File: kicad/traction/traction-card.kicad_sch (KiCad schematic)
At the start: 301 parts, among them Y1 CX3225GA40000D0PTVCC

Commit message: Rev A.17: round 18 — three rechecks of 4425af9 (F190-F198): diversion diodes on the amplifier node (loop passes RSX), diode cell cathode = pin 1 on all 35 diodes, exciter TVS/PTC rows at worst corners + ECU-asleep sustained short (WARN rows, layout rule, QP-RX-04 2b gate), anti-surge RSX, NCV4276C reverse current = QP-RX-05 gate + VR-33, IR-16/IR-42, firmware FW-34..36 (sample freshness, cadence-locked resolver frames, latency sign) + three self-found instances
Co-Authored-By: Claude Fable 5.1 <noreply@anthropic.com>
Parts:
- DBAT, DCLR, DEXN, DEXP, DFLT1, DFLT2, DFO, DIGN, DREVC, DTVSC, DTVSC2, ZLVS, ZSET: symbol traction:D -> traction:D_21
- RSXN, RSXP: MPN ERJ-8ENF2R20V -> ESR18EZPF2R20
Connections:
- net ASC_SET_N: now also ZSET.1; no longer ZSET.2
- net BATSNS: now also DBAT.1; no longer DBAT.2
- net DGND: now also DTVSC2.1, ZSET.2; no longer DTVSC2.2, ZSET.1
- net FAULT_OUT: now also DFO.2; no longer DFO.1
- net FCO: now also DREVC.2, DTVSC.1; no longer DREVC.1, DTVSC.2
- net FLT_CLR_N: now also DCLR.2; no longer DCLR.1
- net FLT_CMB_N: now also DFLT1.2, DFLT2.2; no longer DFLT1.1, DFLT2.1
- net FLT_HS_N: now also DFLT1.1; no longer DFLT1.2
- net FLT_LS_N: now also DFLT2.1; no longer DFLT2.2
- net FOUT_K: now also DFO.1; no longer DFO.2
- net IGN_D: now also DIGN.1; no longer DIGN.2
- net KL15: now also DIGN.2; no longer DIGN.1
- net LVS_G: now also ZLVS.2; no longer ZLVS.1
- net NRC: now also DREVC.1, ZLVS.1; no longer DREVC.2, ZLVS.2
- net TVSM: now also DTVSC.2, DTVSC2.2; no longer DTVSC.1, DTVSC2.1
- net V5A: now also DCLR.1; no longer DCLR.2
- net VBATC: now also DBAT.2; no longer DBAT.1
- net VEXD: now also DEXN.1, DEXP.1; no longer DEXN.2, DEXP.2
- net VREX_N: now also DEXN.2
- net VREX_NX: no longer DEXN.1
- net VREX_P: now also DEXP.2
- net VREX_PX: no longer DEXP.1
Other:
- note added: "rev A.17 - 26 sections - 301 components"
- note removed: "rev A.16 - 26 sections - 301 components"
- moved on the sheet: CEXA1, CEXA2, CEXA3, CEXA4, FEXN, FEXP, REXA1, REXA2, REXA3, REXA4, RSXN, RSXP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

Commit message: Rev A.18: round 19 — three rechecks of e315bf1 (F199-F204): PTC-current row at every permitted voltage (IR-16 0.08/0.14/0.37/0.26 Ω), ≥8 A TVS energy an explicit assumption + QP-RX-04 release criterion, window criterion fixed, exciter TVS → SMDJ7.0A-HRA (coupled island holds the 7.0 V class at a parked 12 V battery / the Marine rail), shared exciter-fault model run for the Marine port (QP-MA-11, kit-loom rule), FW-35 rewritten on an SWG-anchored time origin with clock-derived resync and bounded restart
Co-Authored-By: Claude Fable 5.1 <noreply@anthropic.com>
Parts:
- TVSEN, TVSEP: value SMDJ8.5A-HRA -> SMDJ7.0A-HRA; MPN SMDJ8.5A-HRA -> SMDJ7.0A-HRA
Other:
- note added: "rev A.18 - 26 sections - 301 components"
- note removed: "rev A.17 - 26 sections - 301 components"
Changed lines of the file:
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@@
 		(title "Traction Inverter — Control Card (S32K396 + FS26, ASIL D)")
 		(date "2026-09-23")
-		(rev "A.17")
+		(rev "A.18")
 		(company "Traction Inverter 220 kW pk - Control card (LV), sheet 4 of 4")
 		(comment 1 "Inverter = Power board + Cap bank busbar + bolt-on Discharge board (all HV) + Control card (LV); safe state holds with any link lost")
@@
 		(exclude_from_sim no) (in_bom yes) (on_board yes) (dnp no)
 		(property "Reference" "TVSEN" (at 849.63 173.736 0) (effects (font (size 1.27 1.27))))
-		(property "Value" "SMDJ8.5A-HRA" (at 849.63 182.118 0) (effects (font (size 1.27 1.27))))
+		(property "Value" "SMDJ7.0A-HRA" (at 849.63 182.118 0) (effects (font (size 1.27 1.27))))
 		(property "Footprint" "SMC" (at 849.63 177.8 0) (effects (font (size 1.27 1.27)) (hide yes)))
 		(property "Datasheet" "~" (at 849.63 177.8 0) (effects (font (size 1.27 1.27)) (hide yes)))
 		(property "LCSC" "CLASS" (at 849.63 177.8 0) (effects (font (size 1.27 1.27)) (hide yes)))
-		(property "MPN" "SMDJ8.5A-HRA" (at 849.63 177.8 0) (effects (font (size 1.27 1.27)) (hide yes)))
+		(property "MPN" "SMDJ7.0A-HRA" (at 849.63 177.8 0) (effects (font (size 1.27 1.27)) (hide yes)))
 		(instances (project "traction" (path "/05063e63-3076-48d3-a84c-7e92d29634e7/073bda8d-ada5-42f5-b7f9-206abe13de00" (reference "TVSEN") (unit 1)) (path "/806594cd-32aa-475d-95e3-87c882c626ff" (reference "TVSEN") (unit 1))))
 	)
@@
 		(exclude_from_sim no) (in_bom yes) (on_board yes) (dnp no)
 		(property "Reference" "TVSEP" (at 849.63 143.256 0) (effects (font (size 1.27 1.27))))
-		(property "Value" "SMDJ8.5A-HRA" (at 849.63 151.638 0) (effects (font (size 1.27 1.27))))
+		(property "Value" "SMDJ7.0A-HRA" (at 849.63 151.638 0) (effects (font (size 1.27 1.27))))
 		(property "Footprint" "SMC" (at 849.63 147.32 0) (effects (font (size 1.27 1.27)) (hide yes)))
 		(property "Datasheet" "~" (at 849.63 147.32 0) (effects (font (size 1.27 1.27)) (hide yes)))
 		(property "LCSC" "CLASS" (at 849.63 147.32 0) (effects (font (size 1.27 1.27)) (hide yes)))
-		(property "MPN" "SMDJ8.5A-HRA" (at 849.63 147.32 0) (effects (font (size 1.27 1.27)) (hide yes)))
+		(property "MPN" "SMDJ7.0A-HRA" (at 849.63 147.32 0) (effects (font (size 1.27 1.27)) (hide yes)))
 		(instances (project "traction" (path "/05063e63-3076-48d3-a84c-7e92d29634e7/073bda8d-ada5-42f5-b7f9-206abe13de00" (reference "TVSEP") (unit 1)) (path "/806594cd-32aa-475d-95e3-87c882c626ff" (reference "TVSEP") (unit 1))))
 	)
@@
 	(text "CARD-IF   -   1 section" (exclude_from_sim no) (at 849.63 548.64 0) (effects (font (size 1.524 1.524)) (justify left bottom)))
 	(text "VEHICLE-IF   -   1 section" (exclude_from_sim no) (at 849.63 556.26 0) (effects (font (size 1.524 1.524)) (justify left bottom)))
-	(text "rev A.17   -   26 sections   -   301 components" (exclude_from_sim no) (at 849.884 572.77 0) (effects (font (size 1.524 1.524)) (justify left bottom)))
+	(text "rev A.18   -   26 sections   -   301 components" (exclude_from_sim no) (at 849.884 572.77 0) (effects (font (size 1.524 1.524)) (justify left bottom)))
 	(text "NET NAMING" (exclude_from_sim no) (at 849.884 600.964 0) (effects (font (size 2.0066 2.0066) (bold yes)) (justify left bottom)))
 	(text "internal junctions are named for what they join" (exclude_from_sim no) (at 849.884 607.568 0) (effects (font (size 1.524 1.524)) (justify left bottom)))

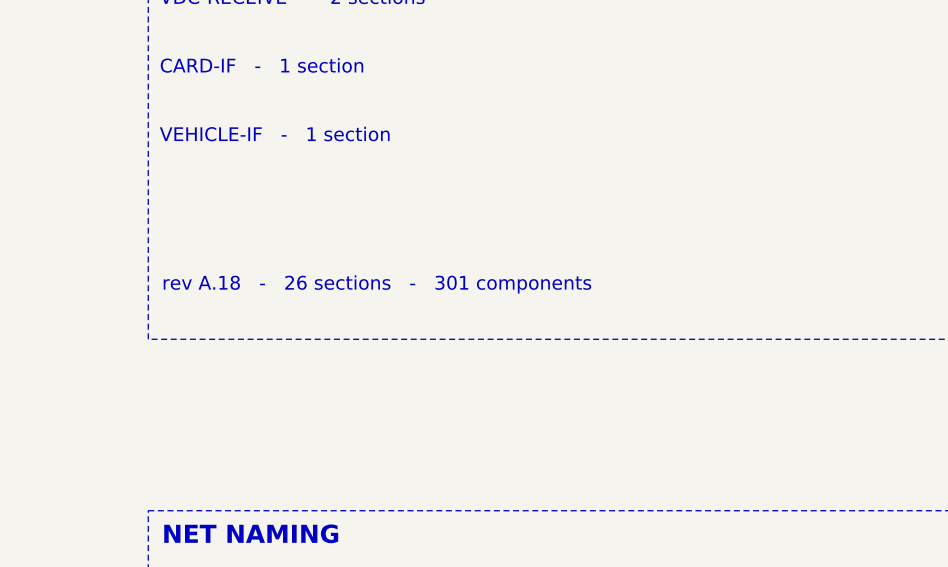
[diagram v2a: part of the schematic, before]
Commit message: Rev A.19: round 20 — three rechecks of 00f6252 (F205-F207): TVS alternate to the 7.0 V class + lock, 4XX discharge alternate 470→220 Ω + lock, T-05/T-06 firmware ID, 8.5 V-era figures re-derived at the IR-16 allocations
Co-Authored-By: Claude Fable 5.1 <noreply@anthropic.com>
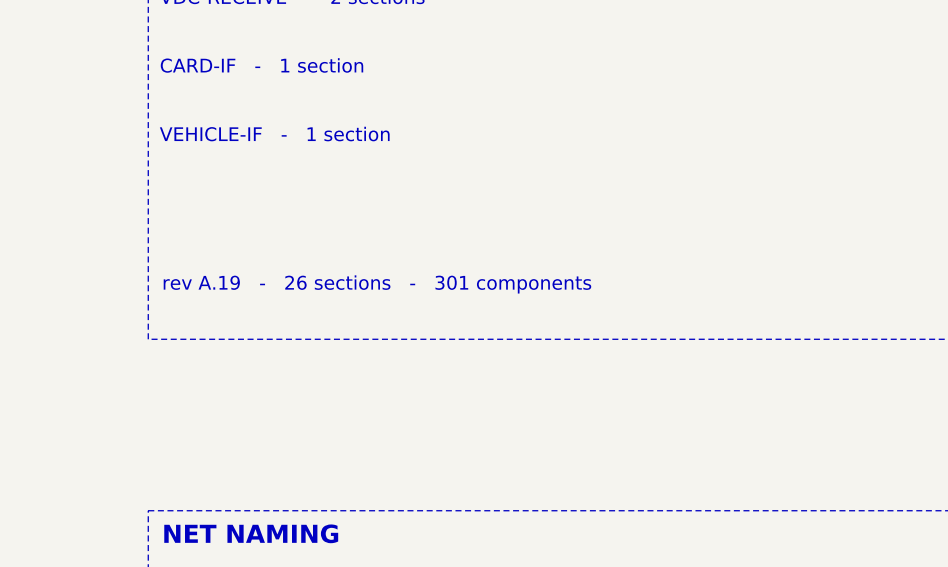
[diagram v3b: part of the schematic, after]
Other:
- note added: "rev A.19 - 26 sections - 301 components"
- note removed: "rev A.18 - 26 sections - 301 components"
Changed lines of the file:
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@@
 		(title "Traction Inverter — Control Card (S32K396 + FS26, ASIL D)")
 		(date "2026-09-23")
-		(rev "A.18")
+		(rev "A.19")
 		(company "Traction Inverter 220 kW pk - Control card (LV), sheet 4 of 4")
 		(comment 1 "Inverter = Power board + Cap bank busbar + bolt-on Discharge board (all HV) + Control card (LV); safe state holds with any link lost")
@@
 	(text "CARD-IF   -   1 section" (exclude_from_sim no) (at 849.63 548.64 0) (effects (font (size 1.524 1.524)) (justify left bottom)))
 	(text "VEHICLE-IF   -   1 section" (exclude_from_sim no) (at 849.63 556.26 0) (effects (font (size 1.524 1.524)) (justify left bottom)))
-	(text "rev A.18   -   26 sections   -   301 components" (exclude_from_sim no) (at 849.884 572.77 0) (effects (font (size 1.524 1.524)) (justify left bottom)))
+	(text "rev A.19   -   26 sections   -   301 components" (exclude_from_sim no) (at 849.884 572.77 0) (effects (font (size 1.524 1.524)) (justify left bottom)))
 	(text "NET NAMING" (exclude_from_sim no) (at 849.884 600.964 0) (effects (font (size 2.0066 2.0066) (bold yes)) (justify left bottom)))
 	(text "internal junctions are named for what they join" (exclude_from_sim no) (at 849.884 607.568 0) (effects (font (size 1.524 1.524)) (justify left bottom)))

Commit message: Rev A.20: round 21 — three rechecks of 551c405 (F208): stale 0.29 Ω in gate ㉘ and the QP-RX-04 fixture instruction → 0.37 Ω, last 8.5 V-era figures aligned, Marine sweep cross-references at the current values
Co-Authored-By: Claude Fable 5.1 <noreply@anthropic.com>
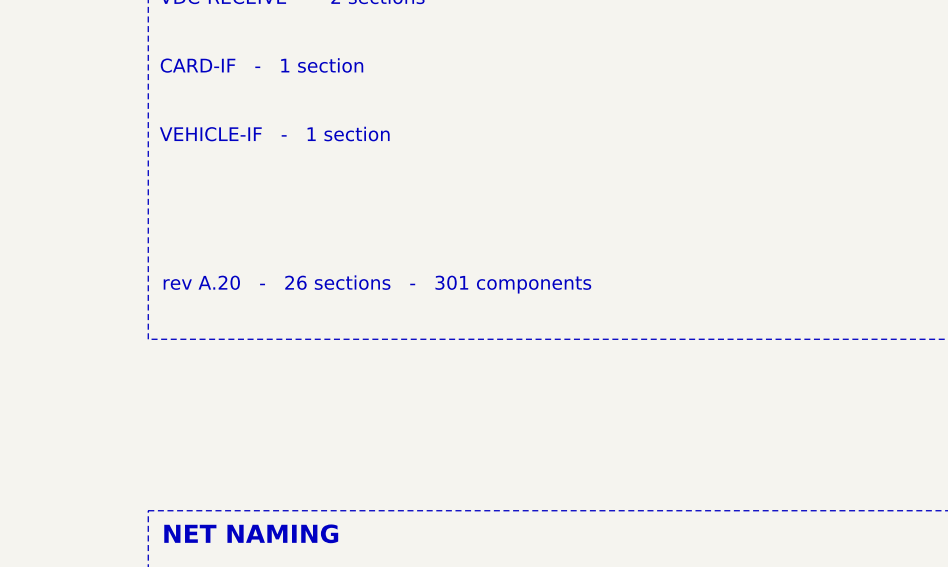
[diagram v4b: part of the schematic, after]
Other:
- note added: "rev A.20 - 26 sections - 301 components"
- note removed: "rev A.19 - 26 sections - 301 components"
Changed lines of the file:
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@@
 		(title "Traction Inverter — Control Card (S32K396 + FS26, ASIL D)")
 		(date "2026-09-23")
-		(rev "A.19")
+		(rev "A.20")
 		(company "Traction Inverter 220 kW pk - Control card (LV), sheet 4 of 4")
 		(comment 1 "Inverter = Power board + Cap bank busbar + bolt-on Discharge board (all HV) + Control card (LV); safe state holds with any link lost")
@@
 	(text "CARD-IF   -   1 section" (exclude_from_sim no) (at 849.63 548.64 0) (effects (font (size 1.524 1.524)) (justify left bottom)))
 	(text "VEHICLE-IF   -   1 section" (exclude_from_sim no) (at 849.63 556.26 0) (effects (font (size 1.524 1.524)) (justify left bottom)))
-	(text "rev A.19   -   26 sections   -   301 components" (exclude_from_sim no) (at 849.884 572.77 0) (effects (font (size 1.524 1.524)) (justify left bottom)))
+	(text "rev A.20   -   26 sections   -   301 components" (exclude_from_sim no) (at 849.884 572.77 0) (effects (font (size 1.524 1.524)) (justify left bottom)))
 	(text "NET NAMING" (exclude_from_sim no) (at 849.884 600.964 0) (effects (font (size 2.0066 2.0066) (bold yes)) (justify left bottom)))
 	(text "internal junctions are named for what they join" (exclude_from_sim no) (at 849.884 607.568 0) (effects (font (size 1.524 1.524)) (justify left bottom)))

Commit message: Rev A.21: round 22 — three rechecks of 0ff44d9 (F209) + the layout handoff (F210–F213): every KiCad symbol bound to a footprint in a shipped traction.pretty (45 verbatim KiCad-10 patterns + 18 datasheet-drawn), fp-lib-table and per-board projects in all sets, pad-per-pin KiCad proof; NCV4276C 5-lead lands, ALM2402/TPS55340 thermal-pad pins, 2-pad crystal; QP §0.2 baseline and stale IDs; docs/layout-handoff.md
Co-Authored-By: Claude Fable 5.1 <noreply@anthropic.com>
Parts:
- CAND1, CAND2, CASCG, CBAL, CBTC, CBTP, CCAN1, CCAN2, CCLR, CCOSA1, CCOSA2, CCOSA3, CCOSD, CCOSF1, CCOSF2, CCT1, CCT2, CEXA1, CEXA2, CEXA3, CEXA4, CEXM, CFLTD, CFLTF, CFLTF2, CIGN, CIGNS, CILK, CLAT, CLAT2, CLDEC, CLVSM, CMA1, CMA2, CMD1, CMD10, CMD11, CMD12, CMD2, CMD3, CMD4, CMD5, CMD6, CMD7, CMD8, CMD9, CMT1F, CMT2F, COF1, COR1, COR2, CRST, CSCH, CSCH2, CSCH3, CSINA1, CSINA2, CSINA3, CSIND, CSINF1, CSINF2, CSNUF, CSNVF, CSNWF, CTAMBF, CTHSF, CUB1, CUB2, CUS1, CUS2, CV25, CVB1, CVB2, CVD1, CVD2, CVDIG, CVM1, CVM2, CVS1, CVS2, CWB1, CWB2, CWS1, CWS2, CYA, CYB: footprint C0603 -> traction:C_0603_1608Metric
- CEXD, CLVC1: footprint C1206 -> traction:C_1206_3216Metric
- CLDE, CLVC2: footprint C1210 -> traction:C_1210_3225Metric
- CLVC3: footprint CAP-ALU-SMD-G-10x10.2 -> traction:CP_Elec_10x10.5
- CSB1, CSB2, CSB3, CSB3B, CSB4, CSB5, CSB6, CSB7, CSB8, CVBOS: footprint C0805 -> traction:C_0805_2012Metric
- DBAT, DCLR, DFLT1, DFLT2, DFO, ZLVS, ZSET: footprint SOD123 -> traction:D_SOD-123
- DCOSP, DSINP, QBAL, QLVN, TVSC1, TVSC2: footprint SOT23 -> traction:SOT-23-3
- DEXN, DEXP: footprint SOD128 -> traction:D_SOD-128
- DIGN, TVSM1, TVSM2: footprint SMA -> traction:D_SMA
- DREVC, DTVSC, DTVSC2, TVSEN, TVSEP: footprint SMC -> traction:D_SMC
- FEXN, FEXP: footprint 1812 -> traction:Fuse_1812_4532Metric
- FLVC: footprint 2410 -> traction:Bel_0680L_2410
- FMT1, FMT2: footprint F0603 -> traction:Fuse_0603_1608Metric
- FVBH, FVBL: footprint PTC2920 -> traction:Fuse_2920_7451Metric
- FVS1: footprint PTC1812 -> traction:Fuse_1812_4532Metric
- JICC: footprint HDR2x20-2.54 -> traction:Samtec_IPL1-120_2x20
- JLEM: footprint HDR2x5 -> traction:PinHeader_2x05_P2.00mm_Vertical
- JSWD: footprint HDR2x5-1.27 -> traction:PinHeader_2x05_P1.27mm_Vertical
- JVEH: footprint AMPSEAL23 -> traction:TE_770669-1
- LCAN1, LCAN2: footprint CMC1210 -> traction:TDK_ACT45B
- LCOR: footprint XAL4020 -> traction:L_Coilcraft_XAL4020-XXX
- LFC: footprint FB1206 -> traction:L_1206_3216Metric
- LSBC: footprint XAL4040 -> traction:L_Coilcraft_XAL4040-XXX
- LUB, LVB, LWB: footprint FB0805 -> traction:L_0805_2012Metric
- LVS1, LVS2, LVS3, LVS4: footprint FB0603 -> traction:L_0603_1608Metric
- QLVS: footprint SOT223 -> traction:SOT-223
- RAGT: footprint R0805 -> traction:R_0805_2012Metric
- RARB, RASCP, RBOOT, RCOS1, RCOS2, RCOSF1, RCOSF2, RCOSR1, RCOSR2, RCPD0, RCPD1, RCPD2, RCPD3, RCT1A, RCT1B, RCT2A, RCT2B, RDBG, RDRB, RENP1, REXA1, REXA2, REXA3, REXA4, REXB1, REXB2, REXB3, REXB4, REXM1, REXM2, REXM3, REXM4, RFCB, RFLTC, RFLTD, RFLTP1, RFLTP2, RFS1, RFS2, RFS3, RGPD, RHWP, RIGN1, RIGN2, RIGNS1, RIGNS2, RILK1, RILK2, RILK3, RILK4, RLAT1, RLAT2, RLDE1, RLDE2, RLVSD, RLVSG, RLVSM, RMRST, RMT1P, RMT1S, RMT2P, RMT2S, ROF1, ROF2, RQDM, RRDB, RRDYP1, RRDYP2, RSB1, RSB2, RSB3, RSB4, RSCH, RSDN, RSIN1, RSIN2, RSINF1, RSINF2, RSINR1, RSINR2, RSNUP, RSNVP, RSNWP, RTAMB, RTAMBP, RTHS, RTHSP, RTMR, RUB0, RUB1, RUB2, RUB3, RV5GP, RV5GS, RVB0, RVB1, RVB2, RVB3, RVD1A, RVD1B, RVD1C, RVD1D, RVD2A, RVD2B, RVD2C, RVD2D, RVM1, RVM2, RVM3, RVM4, RWB0, RWB1, RWB2, RWB3: footprint R0603 -> traction:R_0603_1608Metric
- RFS4, RSXN, RSXP: footprint R1206 -> traction:R_1206_3216Metric
- UAND1, UAND2: footprint SOT363 -> traction:SOT-363_SC-70-6
- UASCG, UOR1, UOR2: footprint SOT353 -> traction:SOT-353_SC-70-5
- UCAN1, UCAN2: footprint SOIC8 -> traction:SOIC-8_3.9x4.9mm_P1.27mm
- UEXD: footprint HTSSOP14-PWP -> traction:ALM2402-Q1_PWP0014H
- UEXF, UMT1, UMT2, UUB1, UUB2, UVB1, UVB2, UVD1, UVD2, UVMB1, UVMB2, UVOF, UWB1, UWB2: footprint SOT23-5 -> traction:SOT-23-5
- ULAT, ULAT2, USCH, USCH2, USCH3: footprint VSSOP8 -> traction:VSSOP-8_2.3x2mm_P0.5mm
- ULDOEX: footprint DPAK5 -> traction:TO-252-5_TabPin3
- UMCU: footprint MAPBGA289 -> traction:MAPBGA-289_14x14mm_Layout17x17_P0.8mm
- USBC: footprint HLQFP48 -> traction:FS26_HLQFP48
- USNSU, USNSV, USNSW: footprint OffBoard -> (none)
- Y1: footprint X3225 -> traction:Kyocera_CX3225GA_2Pad
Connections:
- net AGND: now also UEXD.15 (PAD)
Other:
- note added: "rev A.21 - 26 sections - 301 components"
- note removed: "rev A.20 - 26 sections - 301 components"
- moved on the sheet: CEXD, REXB1, REXB2, REXB3, REXB4, RSDN

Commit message: Rev A.22: round 23 — rechecks of 452de85 (F214–F220), the VESC program (FW-38…FW-46, Traction Tool in Qt) and the "why not done" extension (F221–F239)
Hardware: the R2R reference isolated at ball A9 (RR2R 10 Ω + 1 µF + 100 nF, S32K39 DS note 8), the SWD header on its
surface-mount Samtec land with a mounting-technology lock in the library generator, the footprint library declared
KiCad 10.0.6+ and no longer mirrored into the KiCad 5 sets; the BOM intro follows the SKU; a VREFH window row and VR-34/35.

Firmware (TI_FW_ID 0x0A0F0015, CAL layout 4, 190 fields / 91 CAL rows, 80 DTCs): FW-37 joint torque solve with a
postcondition; the VESC gap closure — FW-38 signed field update (Ed25519, anti-rollback, ISO-TP), FW-39 interlocked motor
self-commissioning, FW-40 UDS diagnostics (0x19/0x22/0x2A/0x14 over ISO 15765-2), FW-41 fault-triggered waveform capture,
FW-42 overspeed, FW-43 run-time statistics, FW-44 key-on offset adoption, FW-45 saturation-dependent inductance tables
with gain scheduling, FW-46 cogging feed-forward; twelve defects found by the closed-loop simulator bridge (F221–F232),
the 64-bit divide out of every ISR path with a link-time guard, the UDS escape single frame accepted by every service,
the root of trust reported (DID 0xFD23), the boot record, motor data and active maps as DIDs; 421 tests / 4937 checks /
0 failed on the host (-O1, -O2, ASan/UBSan, -ffp-contract=off) and on the Cortex-M7 under QEMU with the target compiler
(make qemu-test, T-59); make target-check 63 markers, make target-size with the divide guard.

Traction Tool (tool/): Qt 6 / C++17 Widgets + Qwt, offline; pages Dashboard, Live plots, Controls, Commissioning,
Parameters, Faults & alerts, Analysis, Terminal, Firmware; transports simulator bridge (tool/bridge, the real firmware
against a plant), log replay, CAN (QCanBus with ISO-TP both ways, proved against the firmware over the virtualcan bus);
the signed update end to end over both transports; the commissioning routines, the map sw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
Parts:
- added CR2R1: 1uF, traction:C_0603_1608Metric, symbol traction:C
- added CR2R2: 100nF, traction:C_0603_1608Metric, symbol traction:C
- added RR2R: 10R, traction:R_0603_1608Metric, symbol traction:R
- JSWD: footprint traction:PinHeader_2x05_P1.27mm_Vertical -> traction:Samtec_FTSH-105-01-L-DV-K
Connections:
- net AGND: now also CR2R1.2, CR2R2.2
- net VREF5: now also RR2R.1; no longer UMCU.A9 (A9_VREFH_R2R)
- new net VR2R: CR2R1.1, CR2R2.1, RR2R.2, UMCU.A9 (A9_VREFH_R2R)
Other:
- note added: "rev A.22 - 26 sections - 304 components"
- note removed: "rev A.21 - 26 sections - 301 components"
- moved on the sheet: CAND1, CAND2, CASCG, CBAL, CBTC, CBTP, CCAN1, CCAN2, CCLR, CCOSA1, CCOSA2, CCOSA3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

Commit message: Rev A.23: round 24 — four rechecks of 4ed0101 (F240–F244): the SDADC reference on its supply node, acquisition freshness, the map's flux slope and the ripple limiter's exact bounds, the temperature latch, the V_DC expiry
Hardware (F240, no new part): the S32K39 data sheet's SDADC table (Rev. 3 Table 38, in our archive and our own
extracted-parameters file) requires VREFP within ±25 mV of AVDD; the round-23 disposition had judged the general +100 mV
note and called the figure absent while the references sat on the FS26 VREF, matched to the SDADC-supply LDO only within
±1 %. Every non-R2R reference group (E6/H6 SAR, E10/F13 SDADC) is now on V5A itself with VDDA_SDADC and VDD_HV_A (NXP's
GEN3 arrangement); the ratiometric loads (HW_ID and offset dividers, the seven NTC pull-ups) moved with the reference; the
R2R ladder keeps the FS26 VREF as its isolated supply through the 10 Ω branch (CR2R1 330 nF, 37 kHz); CSB5 2.2 µF holds
the FS26 window alone (1.36–2.92 µF effective); the absolute SAR scale re-budgeted at the LDO2's ±1.75 %; ERC locks, pin
freeze, manifest, handoff §4.11 island rule (≤ 20 mΩ from E12 to any VREFH ball), VR-34 closed by design, IR-26, QP-TH-06.
Pipeline at A.23: ERC 981/0/0, verify 158/18/0, sim 23/6/0, Marine 87/23/0, 21 pages / 2065 pins, KiCad proof PASS, PDFs
and BOMs regenerated (₹72,983 unchanged). The handoff §6 gives every open pre-layout decision a provisional default.

Firmware (TI_FW_ID 0x0A0F0016, CAL layout 4, 191 fields / 92 CAL rows, 82 DTCs): F241 a stopped slow ADC channel stayed
valid forever (the caller discarded the acquisition stamp) → a three-state contract new/held/expired for every slow-list
input with cal_temp_hold_ms and DTC_ADC_SLOW_STALE, every slow consumer audited (V5GD/VOFS, IGN, INTRLOK_N, VSUP, HW_ID);
F242 the inductance map must keep a positive flux slope (≥ 0.25 × L0 below every breakpoint) and the ripple limiter bounds
every piece of its interval in closed form (breakpoints alone shown insufficient by a 20 000-m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
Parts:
- CR2R1: value 1uF -> 330nF; MPN MLCC-1uF-10V-X7R-0603 -> MLCC-330nF-16V-X7R-0603
- CSB5: value 1uF -> 2.2uF; MPN MLCC-1uF-16V-X7R-0805 -> MLCC-2.2uF-16V-X7R-0805
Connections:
- net V5A: now also CMA1.1, CMA2.1, RHWP.1, RMT1P.1, RMT2P.1, ROF1.1, RSNUP.1, RSNVP.1, RSNWP.1, RTAMBP.1, RTHSP.1, UMCU.E10 (E10_VREFH_SDADC_01), UMCU.E6 (E6_VREFH_SAR_456), UMCU.F13 (F13_VREFH_SDADC_23), UMCU.H6 (H6_VREFH_SAR_0123)
- net VREF5: no longer CMA1.1, CMA2.1, RHWP.1, RMT1P.1, RMT2P.1, ROF1.1, RSNUP.1, RSNVP.1, RSNWP.1, RTAMBP.1, RTHSP.1, UMCU.E10 (E10_VREFH_SDADC_01), UMCU.E6 (E6_VREFH_SAR_456), UMCU.F13 (F13_VREFH_SDADC_23), UMCU.H6 (H6_VREFH_SAR_0123)
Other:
- note added: "rev A.23 - 26 sections - 304 components"
- note removed: "rev A.22 - 26 sections - 304 components"
